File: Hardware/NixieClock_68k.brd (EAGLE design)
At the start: 96.8 x 100 mm, 47 parts, among them IC1 68008, IC10 7805, IC11 MIC803, IC12 74HC08N, IC2 AS6C1008, IC3 39SF020, IC4 DS1244Y, IC5 68681, IC6 74HC30N, IC7 74HC04N, IC8 74HC138N, IC9 74HC266N, Q1 3.6864MHz

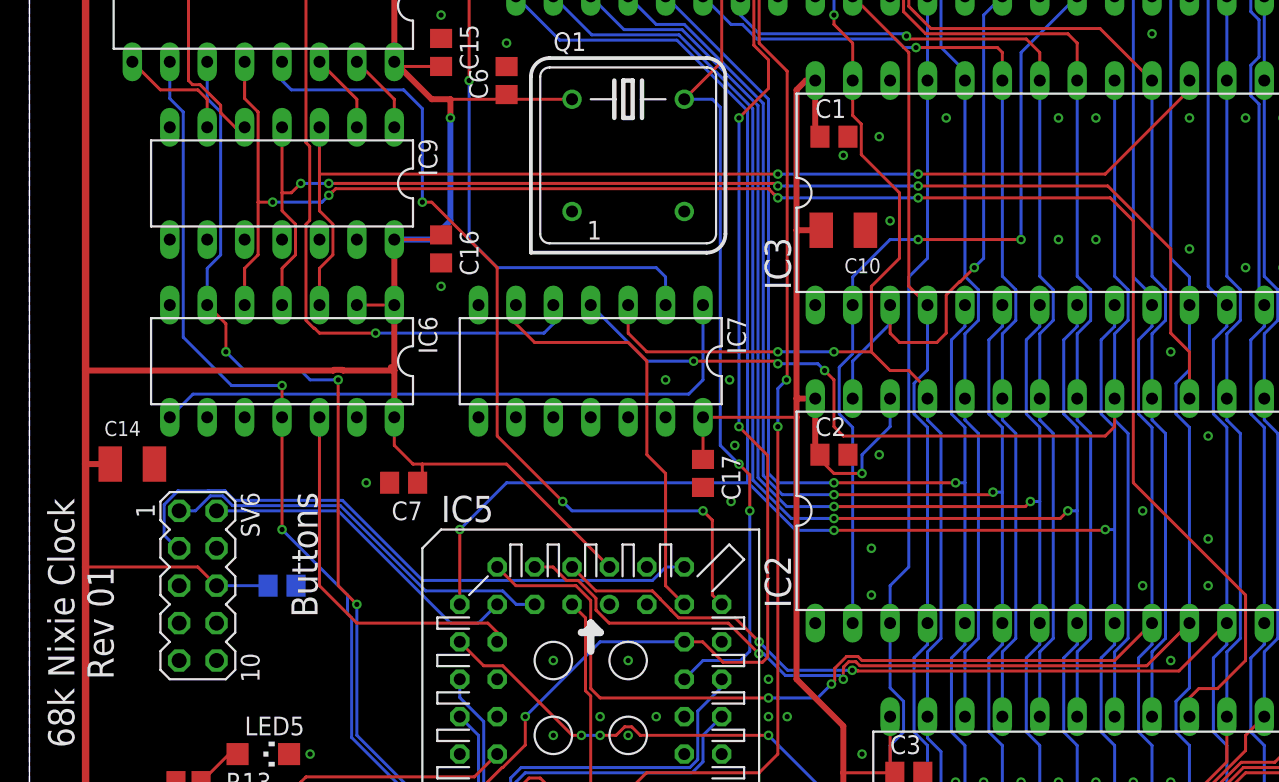
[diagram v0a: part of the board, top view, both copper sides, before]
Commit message: added missing pull-ups to ROM and RAM CS; 68681 DTACK
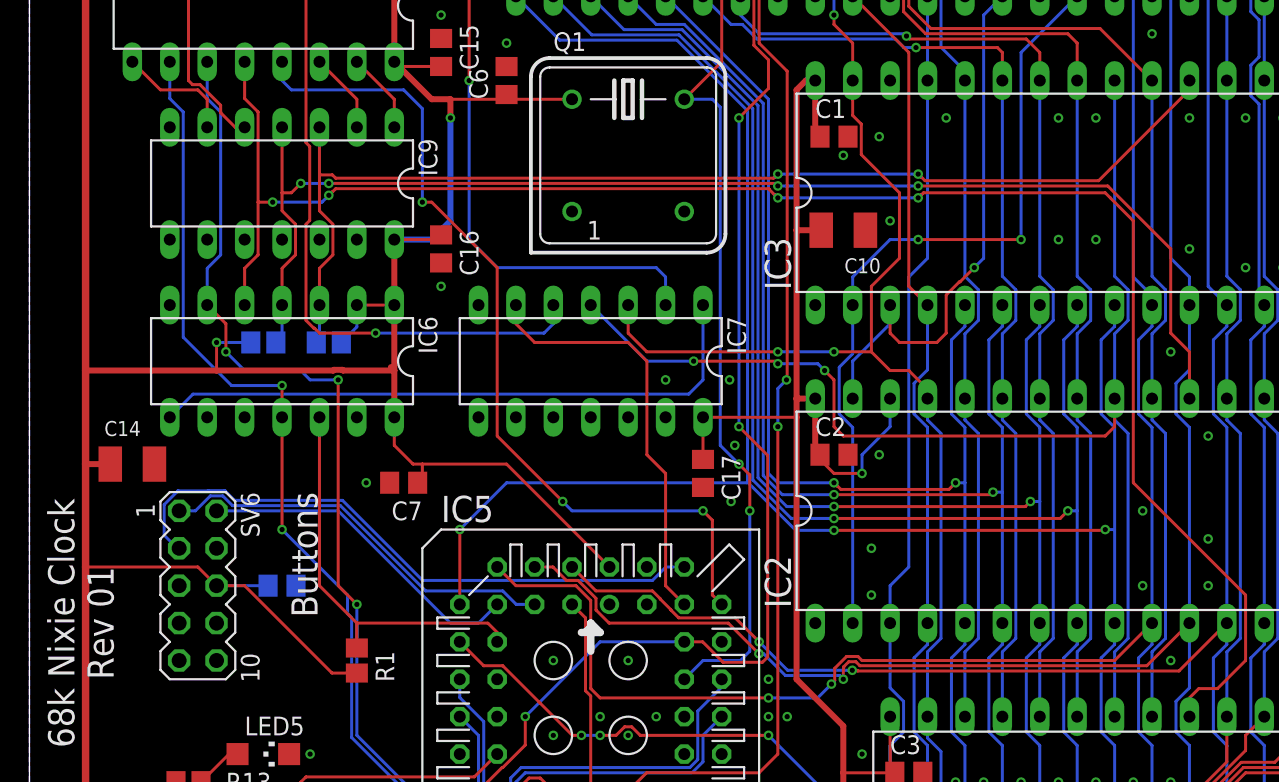
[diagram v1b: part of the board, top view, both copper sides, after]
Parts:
- added R1: 10k, rcl:R2012
- added R2, R3: 3k, rcl:R2012
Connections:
- net !68681_DTACK: now also R1.1
- net !RAM_CS: now also R3.1
- net !ROM_CS: now also R2.1
- net +5V: now also R1.2, R2.2, R3.2
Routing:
- net +5V: track 552.1 -> 571.3 mm, vias 4 -> 5
- net !ROM_CS: track 74.9 -> 78.1 mm
- net !RAM_CS: track 85.9 -> 88.7 mm
- net !68681_DTACK: track 25.4 -> 27.1 mm
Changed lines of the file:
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@@
 <attribute name="VALUE" x="23.876" y="91.44" size="1.27" layer="27" ratio="10" rot="R180"/>
+</element>
+<element name="R1" library="rcl" library_urn="urn:adsk.eagle:library:334" package="R2012" package3d_urn="urn:adsk.eagle:package:23543/2" value="10k" x="22.225" y="34.29" smashed="yes" rot="R270">
+<attribute name="MOUSER" value="652-CR0805FX-1002ELF" x="22.225" y="34.29" size="1.778" layer="27" rot="R270" display="off"/>
+<attribute name="NAME" x="23.495" y="34.925" size="1.27" layer="25" rot="R270"/>
+<attribute name="SPICEPREFIX" value="R" x="22.225" y="34.29" size="1.778" layer="27" rot="R270" display="off"/>
+</element>
+<element name="R2" library="rcl" library_urn="urn:adsk.eagle:library:334" package="R2012" package3d_urn="urn:adsk.eagle:package:23543/2" value="3k" x="20.32" y="55.88" smashed="yes" rot="MR180">
+<attribute name="MOUSER" value="652-CR0805JW-302ELF" x="20.32" y="55.88" size="1.778" layer="28" rot="MR180" display="off"/>
+<attribute name="NAME" x="20.32" y="53.34" size="1.27" layer="26" rot="MR0"/>
+<attribute name="SPICEPREFIX" value="R" x="20.32" y="55.88" size="1.778" layer="28" rot="MR180" display="off"/>
+</element>
+<element name="R3" library="rcl" library_urn="urn:adsk.eagle:library:334" package="R2012" package3d_urn="urn:adsk.eagle:package:23543/2" value="3k" x="15.875" y="55.88" smashed="yes" rot="MR0">
+<attribute name="MOUSER" value="652-CR0805JW-302ELF" x="15.875" y="55.88" size="1.778" layer="28" rot="MR0" display="off"/>
+<attribute name="NAME" x="15.875" y="53.34" size="1.27" layer="26" rot="MR0"/>
+<attribute name="SPICEPREFIX" value="R" x="15.875" y="55.88" size="1.778" layer="28" rot="MR0" display="off"/>
 </element>
 </elements>
@@
 <wire x1="21.2379125" y1="54.023" x2="20.6720875" y2="54.023" width="0.4064" layer="1"/>
 <wire x1="20.6720875" y1="54.023" x2="20.6240875" y2="53.975" width="0.4064" layer="1"/>
-<wire x1="20.6240875" y1="53.975" x2="3.81" y2="53.975" width="0.4064" layer="1"/>
+<wire x1="20.6240875" y1="53.975" x2="12.7" y2="53.975" width="0.4064" layer="1"/>
+<wire x1="12.7" y1="53.975" x2="3.81" y2="53.975" width="0.4064" layer="1"/>
 <wire x1="5.485" y1="47.625" x2="3.81" y2="47.625" width="0.4064" layer="1"/>
+<contactref element="R1" pad="2"/>
+<wire x1="22.225" y1="33.44" x2="20.535" y2="33.44" width="0.2032" layer="1"/>
+<wire x1="20.535" y1="33.44" x2="14.605" y2="39.37" width="0.2032" layer="1"/>
+<wire x1="14.605" y1="39.37" x2="12.7" y2="39.37" width="0.2032" layer="1"/>
+<contactref element="R2" pad="2"/>
+<contactref element="R3" pad="2"/>
+<wire x1="21.17" y1="55.88" x2="22.225" y2="56.935" width="0.2032" layer="16"/>
+<wire x1="22.225" y1="56.935" x2="22.225" y2="58.42" width="0.2032" layer="16"/>
+<wire x1="15.025" y1="55.88" x2="12.7" y2="55.88" width="0.2032" layer="16"/>
+<via x="12.7" y="55.88" extent="1-16" drill="0.35"/>
+<wire x1="12.7" y1="55.88" x2="12.7" y2="53.975" width="0.2032" layer="1"/>
 </signal>
 <signal name="GND">
@@
 <wire x1="62.5856" y1="34.4649375" x2="62.5856" y2="29.4408375" width="0.2032" layer="16"/>
 <via x="54.61" y="46.355" extent="1-16" drill="0.35"/>
-<wire x1="62.865" y1="46.355" x2="54.61" y2="46.355" width="0.2032" layer="1"/>
 <via x="62.865" y="46.355" extent="1-16" drill="0.35"/>
 <wire x1="62.865" y1="46.355" x2="63.5" y2="46.355" width="0.2032" layer="16"/>
@@
 <wire x1="50.165" y1="46.99" x2="50.8" y2="46.355" width="0.2032" layer="16"/>
 <wire x1="50.8" y1="46.355" x2="54.61" y2="46.355" width="0.2032" layer="16"/>
+<wire x1="54.61" y1="46.355" x2="54.8358" y2="46.1292" width="0.2032" layer="1"/>
+<wire x1="54.8358" y1="46.1292" x2="54.850825" y2="46.1292" width="0.2032" layer="1"/>
+<wire x1="54.850825" y1="46.1292" x2="55.076625" y2="45.9034" width="0.2032" layer="1"/>
+<wire x1="62.4134" y1="45.9034" x2="62.865" y2="46.355" width="0.2032" layer="1"/>
+<wire x1="55.076625" y1="45.9034" x2="62.4134" y2="45.9034" width="0.2032" layer="1"/>
 </signal>
 <signal name="A8">
@@
 <wire x1="20.5994" y1="61.8258375" x2="19.685" y2="60.9114375" width="0.2032" layer="1"/>
 <wire x1="78.74" y1="73.66" x2="78.74" y2="73.025" width="0.2032" layer="1"/>
-<wire x1="78.74" y1="73.025" x2="73.025" y2="67.31" width="0.2032" layer="1"/>
-<wire x1="73.025" y1="67.31" x2="60.325" y2="67.31" width="0.2032" layer="1"/>
 <via x="60.325" y="67.31" extent="1-16" drill="0.35"/>
 <wire x1="60.325" y1="67.31" x2="50.8" y2="67.31" width="0.2032" layer="16"/>
 <via x="50.8" y="67.31" extent="1-16" drill="0.35"/>
-<wire x1="50.8" y1="67.31" x2="19.685" y2="67.31" width="0.2032" layer="1"/>
+<wire x1="50.8" y1="67.31" x2="50.5742" y2="67.0842" width="0.2032" layer="1"/>
+<wire x1="50.5742" y1="67.0842" x2="50.559175" y2="67.0842" width="0.2032" layer="1"/>
+<wire x1="50.559175" y1="67.0842" x2="50.505575" y2="67.0306" width="0.2032" layer="1"/>
+<wire x1="20.786625" y1="67.0306" x2="20.560825" y2="67.2564" width="0.2032" layer="1"/>
+<wire x1="19.7386" y1="67.2564" x2="19.685" y2="67.31" width="0.2032" layer="1"/>
+<wire x1="20.560825" y1="67.2564" x2="19.7386" y2="67.2564" width="0.2032" layer="1"/>
+<wire x1="50.505575" y1="67.0306" x2="20.786625" y2="67.0306" width="0.2032" layer="1"/>
+<wire x1="60.791625" y1="66.8584" x2="60.565825" y2="67.0842" width="0.2032" layer="1"/>
+<wire x1="60.565825" y1="67.0842" x2="60.5508" y2="67.0842" width="0.2032" layer="1"/>
+<wire x1="60.5508" y1="67.0842" x2="60.325" y2="67.31" width="0.2032" layer="1"/>
+<wire x1="72.5734" y1="66.8584" x2="60.791625" y2="66.8584" width="0.2032" layer="1"/>
+<wire x1="78.74" y1="73.025" x2="72.5734" y2="66.8584" width="0.2032" layer="1"/>
+<contactref element="R2" pad="1"/>
+<wire x1="19.685" y1="58.42" x2="19.685" y2="56.095" width="0.2032" layer="16"/>
+<wire x1="19.685" y1="56.095" x2="19.47" y2="55.88" width="0.2032" layer="16"/>
 </signal>
 <signal name="!RAM_CS">
@@
 <wire x1="77.47" y1="56.515" x2="78.74" y2="55.245" width="0.2032" layer="1"/>
 <wire x1="78.74" y1="55.245" x2="78.74" y2="52.07" width="0.2032" layer="1"/>
+<contactref element="R3" pad="1"/>
+<wire x1="17.145" y1="58.42" x2="17.145" y2="56.3" width="0.2032" layer="16"/>
+<wire x1="17.145" y1="56.3" x2="16.725" y2="55.88" width="0.2032" layer="16"/>
 </signal>
 <signal name="N$8">
@@
 <wire x1="50.8" y1="65.6956" x2="60.325" y2="65.6956" width="0.2032" layer="16"/>
 <via x="60.325" y="65.6956" extent="1-16" drill="0.35"/>
-<wire x1="60.325" y1="65.6956" x2="73.3694" y2="65.6956" width="0.2032" layer="1"/>
 <wire x1="20.786625" y1="66.3194" x2="50.1762" y2="66.3194" width="0.2032" layer="1"/>
-<wire x1="73.3694" y1="65.6956" x2="74.93" y2="64.135" width="0.2032" layer="1"/>
+<wire x1="73.3694" y1="65.6956" x2="73.66" y2="65.405" width="0.2032" layer="1"/>
+<wire x1="73.66" y1="65.405" x2="74.93" y2="64.135" width="0.2032" layer="1"/>
 <wire x1="74.93" y1="64.135" x2="74.93" y2="46.355" width="0.2032" layer="1"/>
 <wire x1="74.93" y1="46.355" x2="82.55" y2="38.735" width="0.2032" layer="1"/>
@@
 <wire x1="82.55" y1="38.735" x2="82.55" y2="34.29" width="0.2032" layer="1"/>
 <wire x1="82.55" y1="34.29" x2="80.645" y2="32.385" width="0.2032" layer="1"/>
+<wire x1="73.3694" y1="65.6956" x2="73.025" y2="66.04" width="0.2032" layer="1"/>
+<wire x1="73.025" y1="66.04" x2="60.684425" y2="66.04" width="0.2032" layer="1"/>
+<wire x1="60.684425" y1="66.04" x2="60.565825" y2="65.9214" width="0.2032" layer="1"/>
+<wire x1="60.565825" y1="65.9214" x2="60.5508" y2="65.9214" width="0.2032" layer="1"/>
+<wire x1="60.5508" y1="65.9214" x2="60.325" y2="65.6956" width="0.2032" layer="1"/>
 </signal>
 <signal name="!NIXIE_CS">
@@
 <wire x1="31.75" y1="36.195" x2="31.75" y2="35.56" width="0.2032" layer="1"/>
 <wire x1="19.685" y1="39.37" x2="22.225" y2="36.83" width="0.2032" layer="1"/>
+<contactref element="R1" pad="1"/>
+<wire x1="22.225" y1="36.83" x2="22.225" y2="35.14" width="0.2032" layer="1"/>
 </signal>
 <signal name="!RAM_CS0">

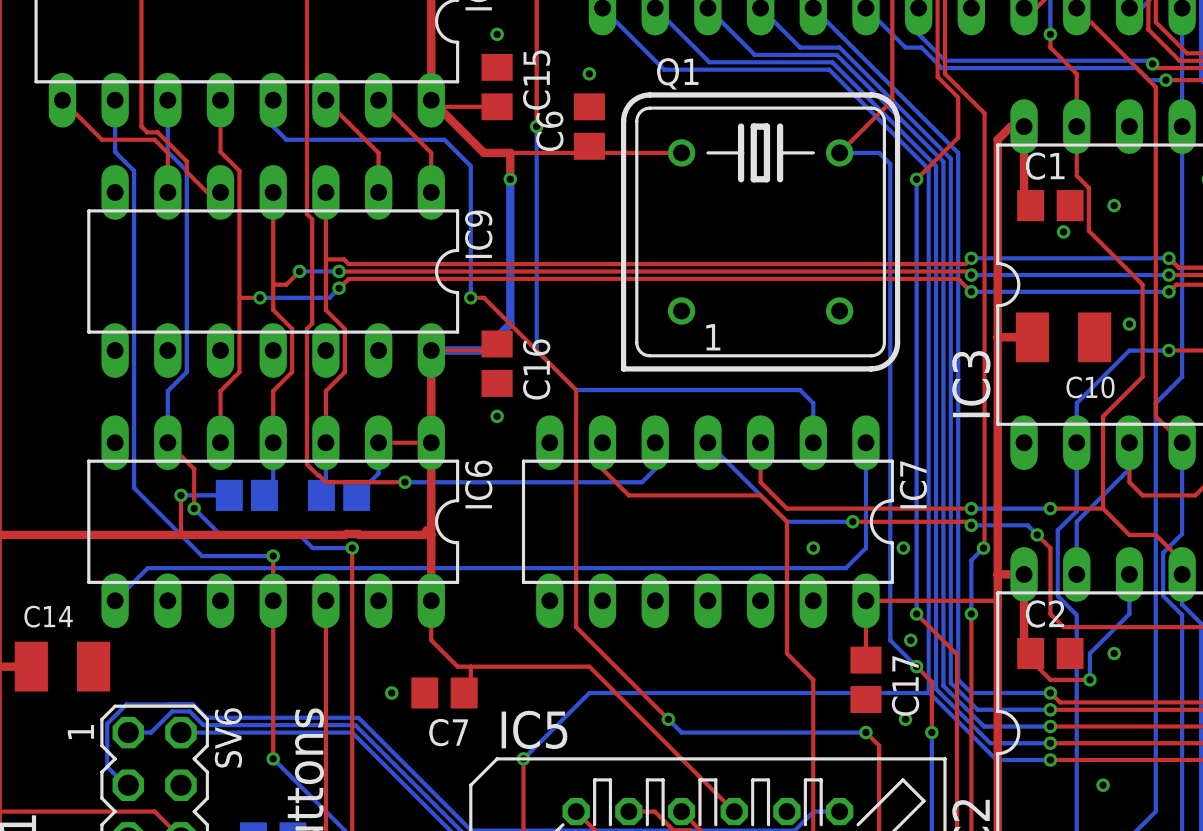
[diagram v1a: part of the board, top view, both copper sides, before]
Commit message: finished tube board schematic
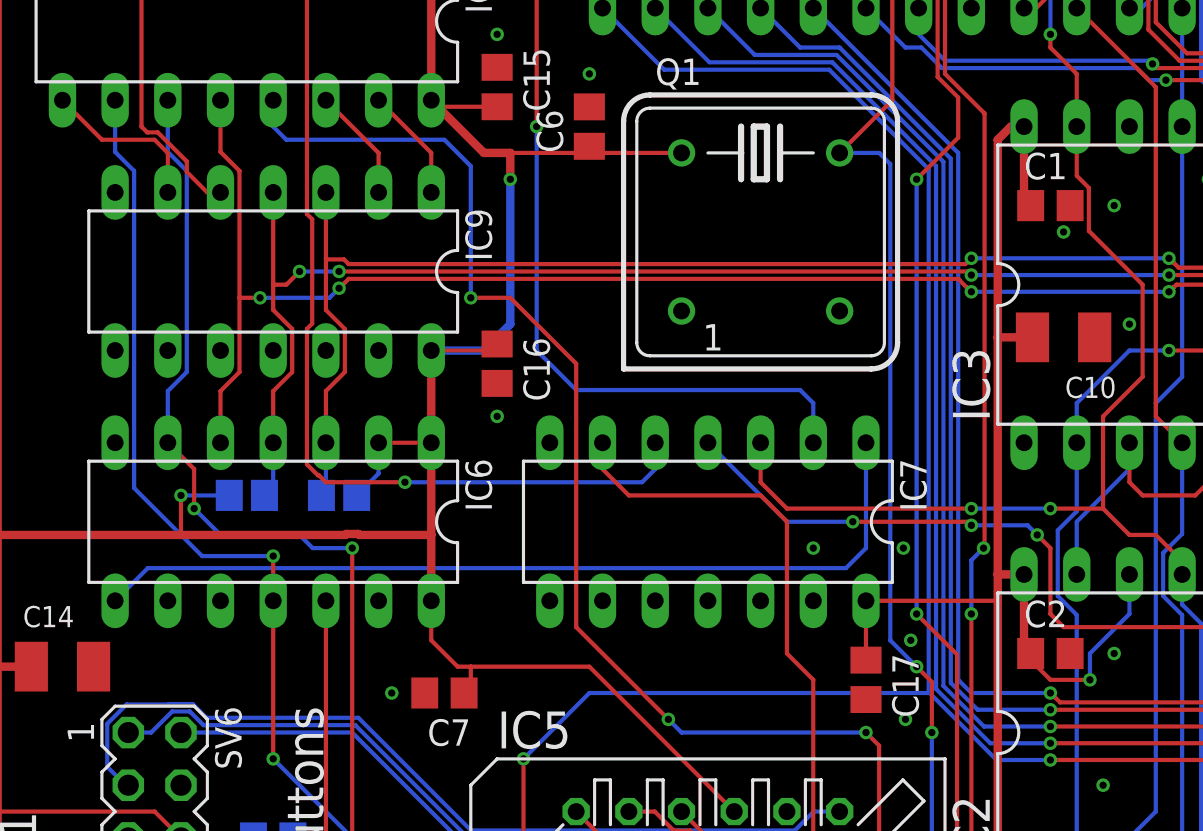
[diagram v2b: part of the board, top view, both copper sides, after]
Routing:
- net R/!W!: track 184.0 -> 182.7 mm
- net !68681_CS: track 59.2 -> 60.0 mm
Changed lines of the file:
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@@
 <wire x1="26.67" y1="47.625" x2="26.67" y2="46.675" width="0.2032" layer="1"/>
 <wire x1="26.67" y1="46.675" x2="26.35" y2="46.355" width="0.2032" layer="1"/>
-<wire x1="24.535" y1="54.205" x2="24.765" y2="53.975" width="0.4064" layer="1"/>
 <wire x1="25.781" y1="83.63124375" x2="25.781" y2="81.46875625" width="0.4064" layer="1"/>
 <wire x1="24.765" y1="86.995" x2="24.765" y2="84.64724375" width="0.4064" layer="1"/>
@@
 <wire x1="60.96" y1="50.6193375" x2="61.8744" y2="49.7049375" width="0.2032" layer="16"/>
 <wire x1="61.8744" y1="49.7049375" x2="61.8744" y2="35.7908375" width="0.2032" layer="16"/>
-<wire x1="55.88" y1="72.39" x2="55.88" y2="73.66" width="0.2032" layer="1"/>
 <wire x1="60.96" y1="30.48" x2="60.96" y2="29.0293375" width="0.2032" layer="16"/>
 <wire x1="61.8744" y1="14.3256" x2="63.5" y2="12.7" width="0.2032" layer="16"/>
@@
 <wire x1="26.6852" y1="39.7256" x2="42.2887625" y2="39.7256" width="0.2032" layer="16"/>
 <wire x1="9.144" y1="44.87084375" x2="9.144" y2="42.799" width="0.2032" layer="16"/>
-<wire x1="10.09475625" y1="45.8216" x2="10.076578125" y2="45.803421875" width="0.2032" layer="16"/>
 <wire x1="10.076578125" y1="45.803421875" x2="9.144" y2="44.87084375" width="0.2032" layer="16"/>
 <wire x1="9.144" y1="42.799" x2="10.033" y2="41.91" width="0.2032" layer="16"/>
@@
 <wire x1="17.78" y1="73.025" x2="17.145" y2="73.66" width="0.2032" layer="16"/>
 <wire x1="17.145" y1="73.66" x2="17.145" y2="74.93" width="0.2032" layer="16"/>
-<wire x1="31.75" y1="49.53" x2="31.75" y2="60.96" width="0.2032" layer="1"/>
-<wire x1="31.75" y1="60.96" x2="27.305" y2="65.405" width="0.2032" layer="1"/>
-<wire x1="27.305" y1="65.405" x2="26.67" y2="65.405" width="0.2032" layer="1"/>
+<wire x1="31.75" y1="49.53" x2="31.75" y2="62.23" width="0.2032" layer="1"/>
+<wire x1="31.75" y1="62.23" x2="28.575" y2="65.405" width="0.2032" layer="1"/>
+<wire x1="28.575" y1="65.405" x2="26.67" y2="65.405" width="0.2032" layer="1"/>
 <wire x1="36.195" y1="45.085" x2="31.75" y2="49.53" width="0.2032" layer="1"/>
 </signal>
